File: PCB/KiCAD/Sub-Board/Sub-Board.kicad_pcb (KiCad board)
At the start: 4 copper layers, 50.5 x 113 mm, 200 parts, among them J1 Conn_02x08, J10 Type, J11 Power/I2C, J12 Address, J13 Power/I2C, J14 Address, J15 GPIO, J16 Type, J17 GPIO, J18 Type, J19 Power/I2C, J2 Conn_01x04_Pin, J20 Address, J21 Power/I2C, J22 Address, J23 GPIO, J24 Type, J25 GPIO, J26 Type, J27 Power/I2C, J28 Address, J29 Power/I2C, J3 Power/I2C, J30 Address, J31 GPIO, J32 Type, J33 GPIO, J34 Type, J4 Address, J5 Power/I2C, J6 Address, J7 GPIO, J8 Type, J9 GPIO, SW1 SW_DIP_x07, U1 TPS629210DRLR, U2 74HC165, U3 STM32F401VETx, U4 74HC165, U5 74HC165, U6 74HC165, U7 74HC165, Y1 26 MHz

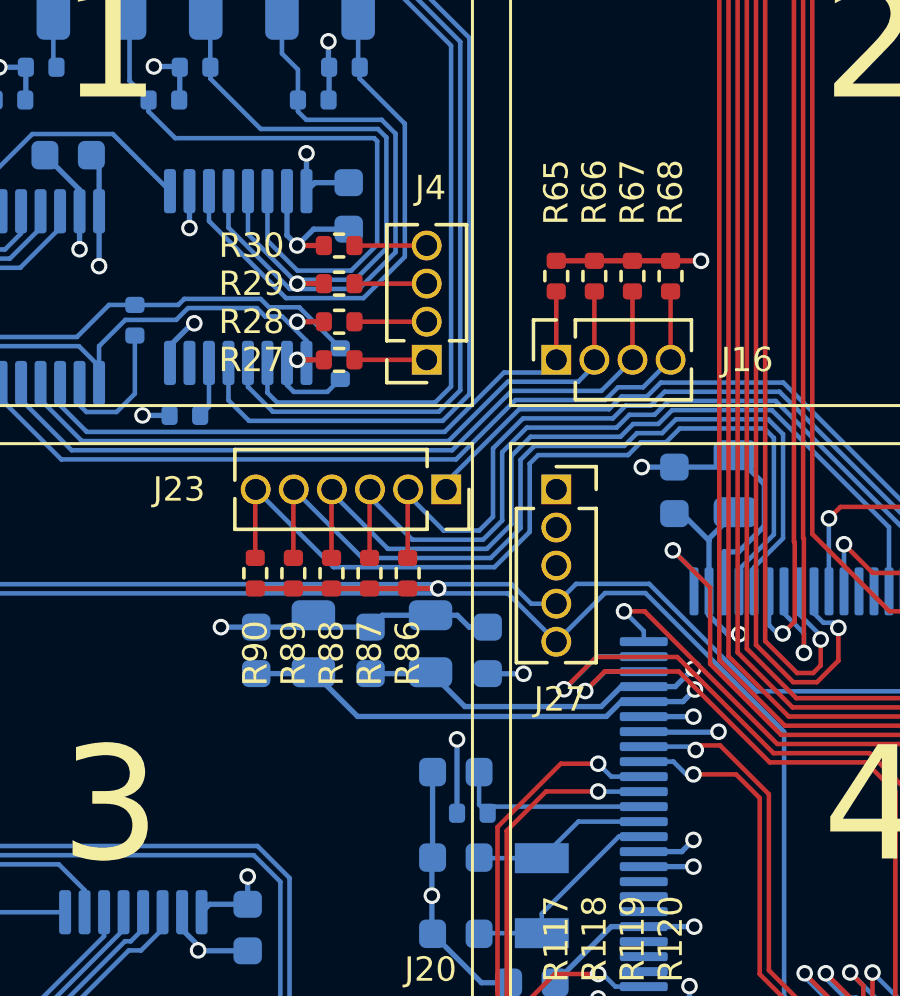
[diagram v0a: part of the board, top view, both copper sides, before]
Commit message: Sub Board: Gerber and BOM files
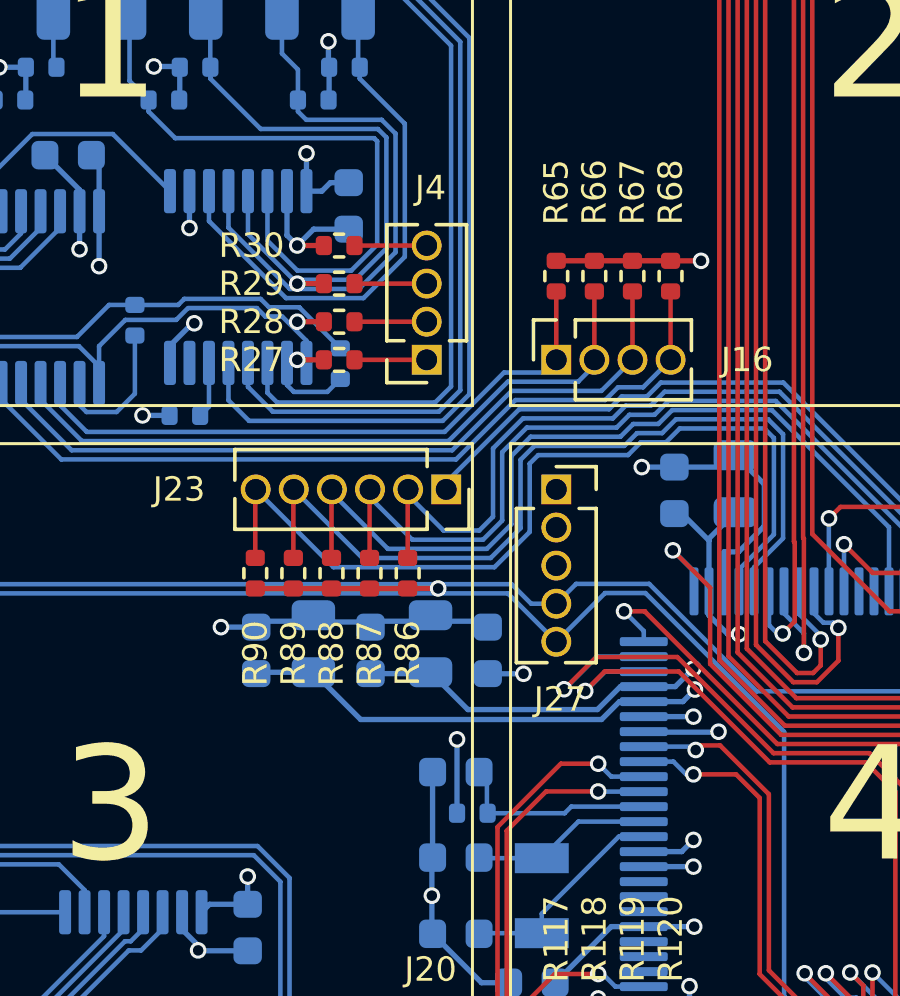
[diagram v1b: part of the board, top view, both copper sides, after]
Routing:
- net /Power Supply/+3.3V Analog: track 147.3 -> 145.6 mm
- net /Power Supply/AREF: track 221.4 -> 220.3 mm
